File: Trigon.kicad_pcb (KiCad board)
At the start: 2 copper layers, 160 x 120 mm, 70 parts, among them J1 USB_C_Receptacle_USB2.0, SW1 SW_Push, SW2 Rotary_Encoder_Switch, U1 ATmega32U4-AU, Y1 16MHz

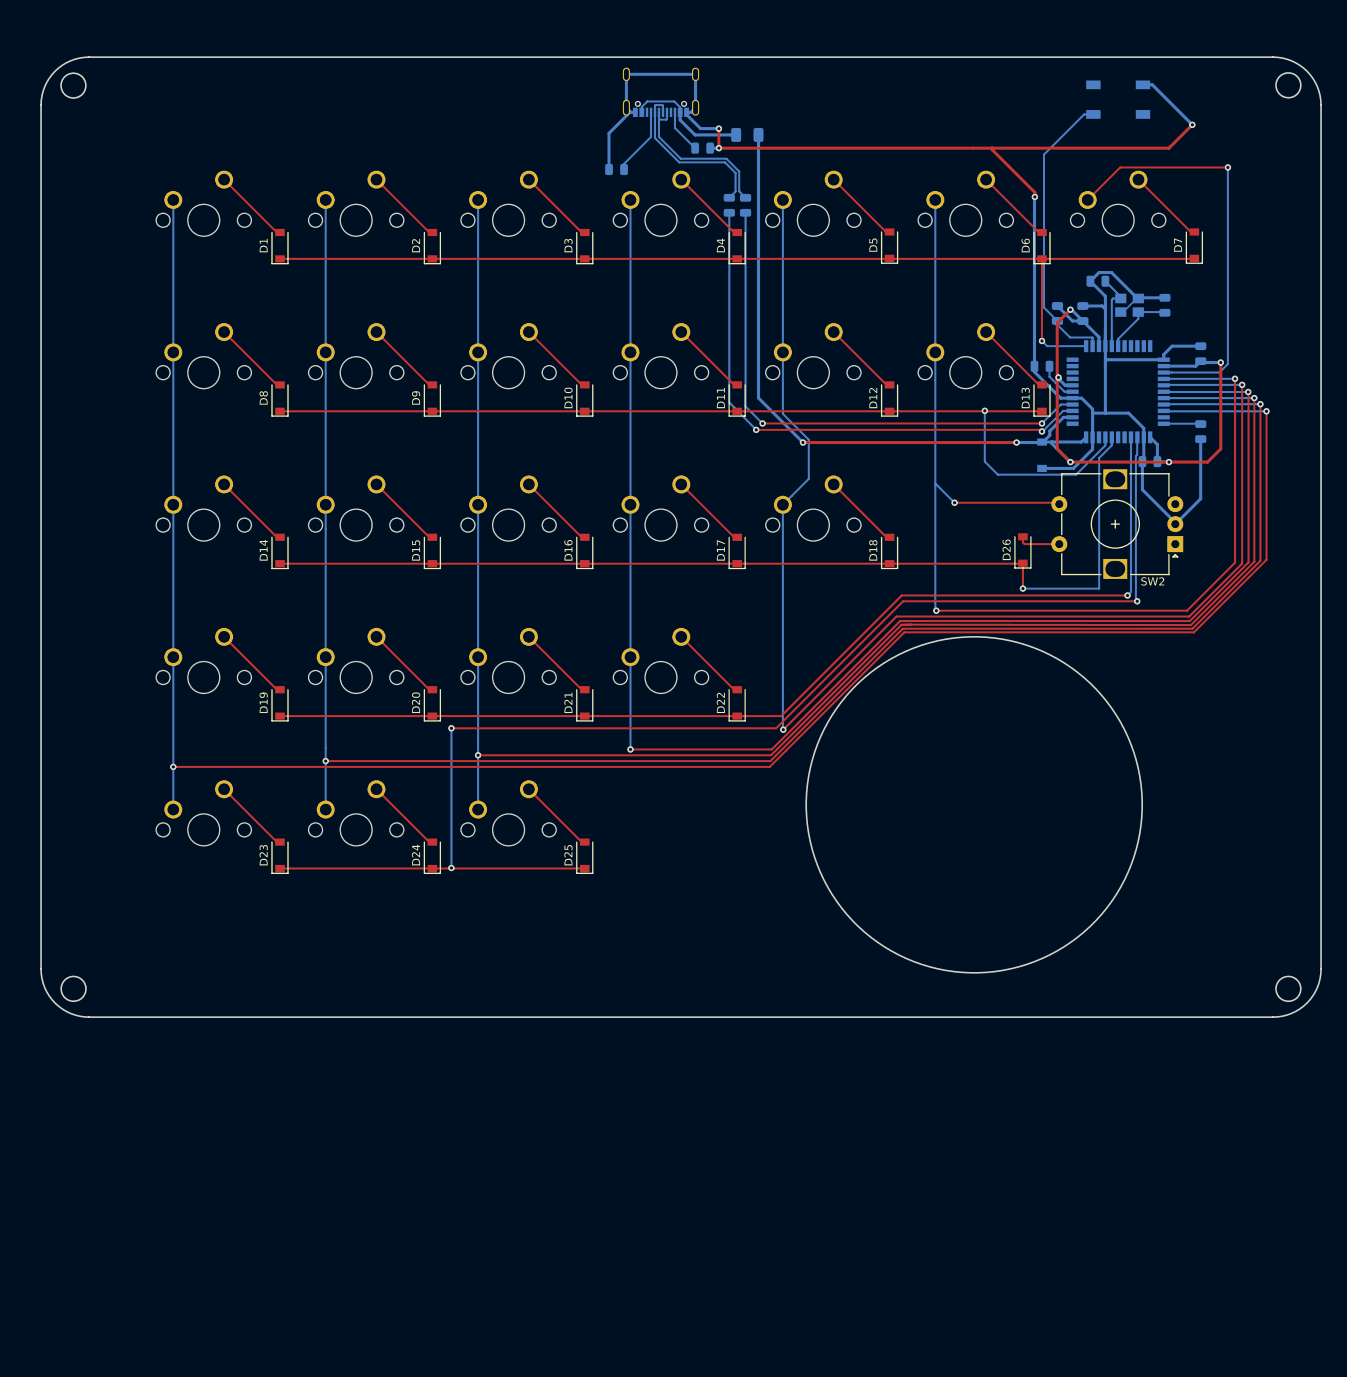
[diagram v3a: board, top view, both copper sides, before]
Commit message: full ground fill
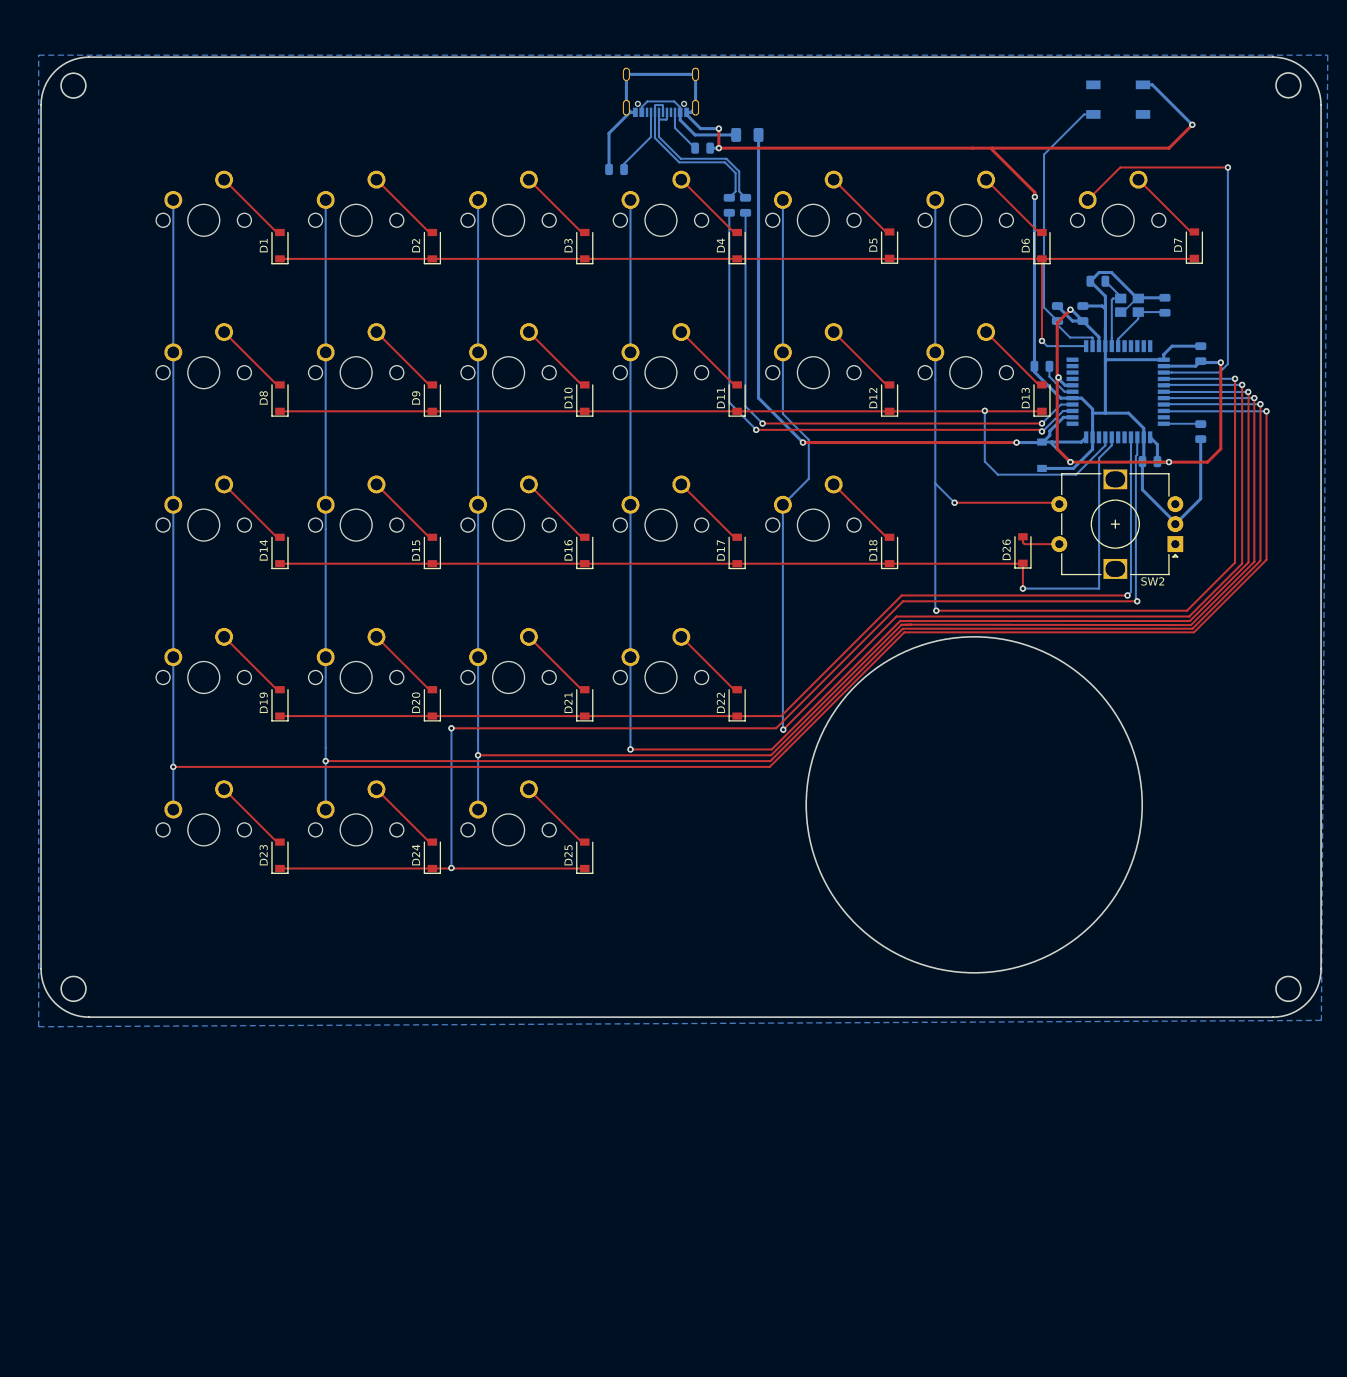
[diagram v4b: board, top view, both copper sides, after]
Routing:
- added copper zone on B.Cu, net (none)
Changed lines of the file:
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@@
   (segment (start 143.6215 -69.81875) (end 143.66875 -69.7715) (width 0.254) (layer B.Cu) (net 57))
   (segment (start 139.05 -69.81875) (end 143.6215 -69.81875) (width 0.254) (layer B.Cu) (net 57))
+  (zone (net 0) (net_name "") (layer B.Cu) (hatch edge 0.508)
+    (connect_pads (clearance 0.508))
+    (min_thickness 0.254)
+    (fill yes (arc_segments 32) (thermal_gap 0.508) (thermal_bridge_width 0.508))
+    (polygon
+      (pts
+        (xy 158.75 4.7625) (xy -1.5875 5.55625) (xy -1.5875 -115.8875) (xy 159.54375 -115.8875)
+      )
+    )
+  )
 )

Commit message: decorative stuff
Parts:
- added G***: LOGO, Trigon:wiggle-mask, B.Cu at (77.7, -57.7)
- added G***: LOGO, Trigon:wiggle, F.Cu at (78.0, -39.4)
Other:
- board text added: "by"
- board text added: "designed"
- board text added: "nk"
- board text added: "rev 0"

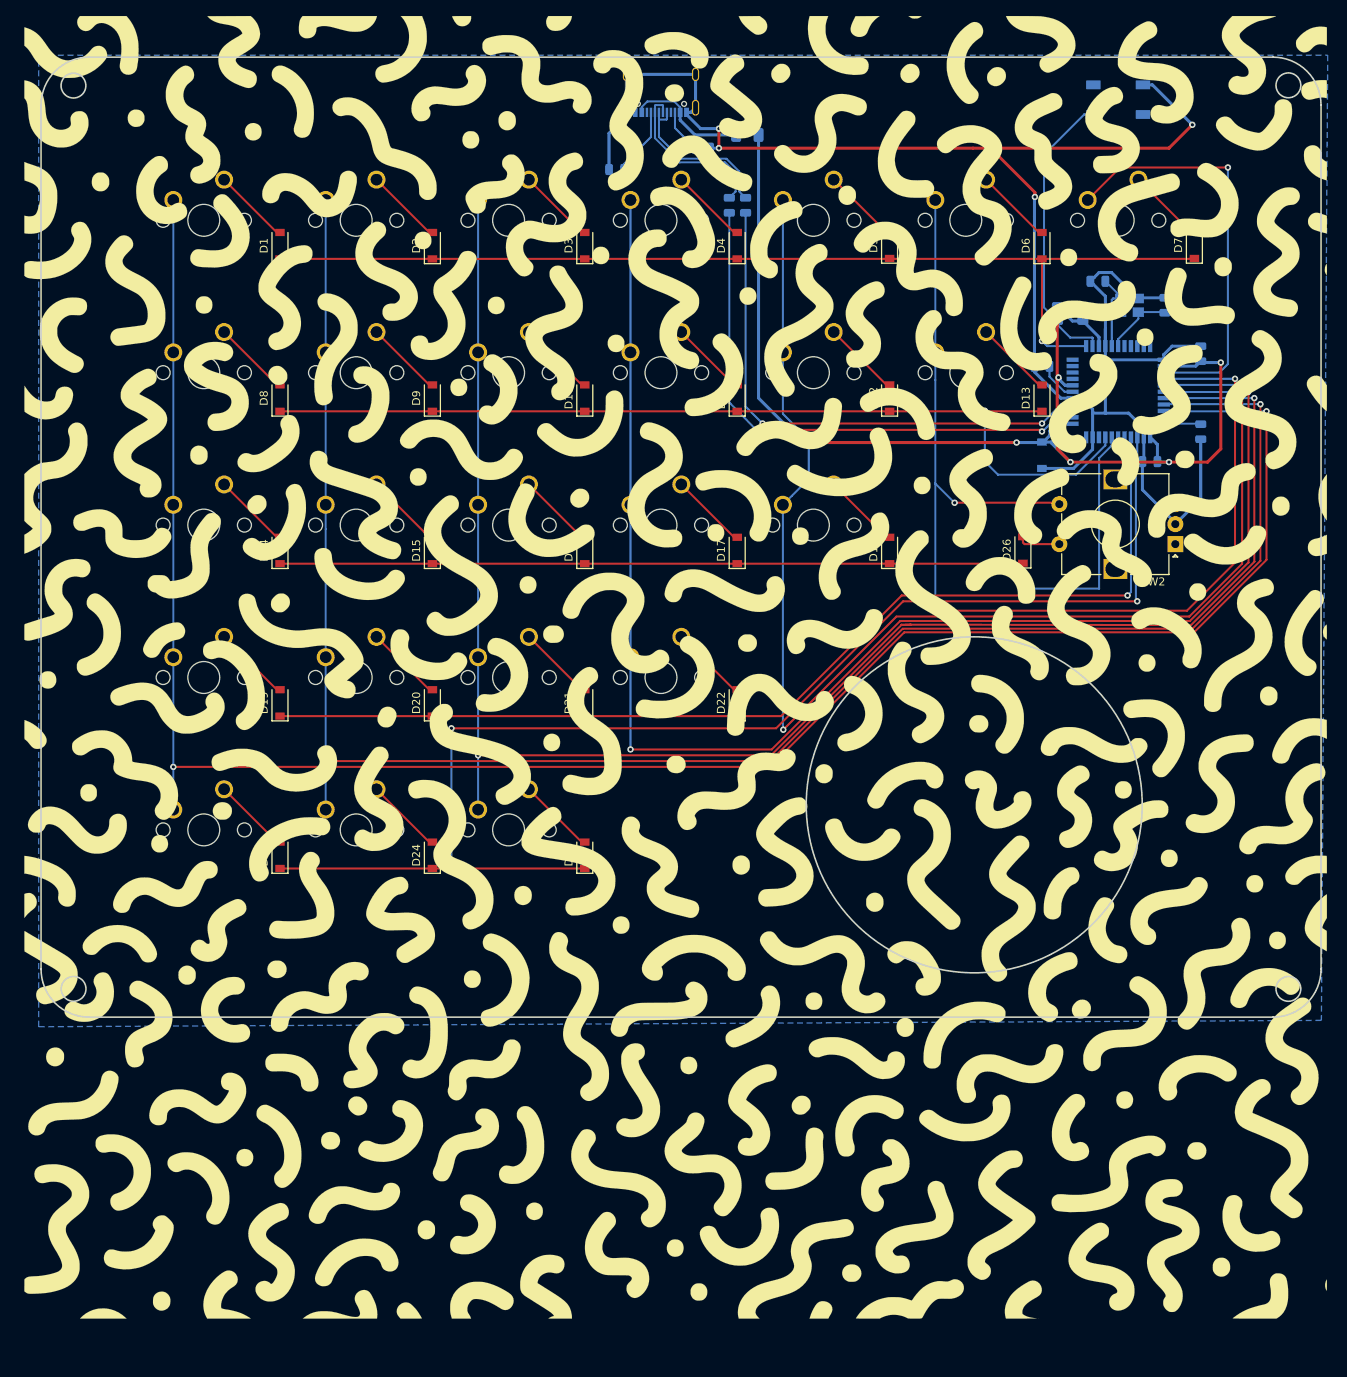
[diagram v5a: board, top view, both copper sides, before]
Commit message: all on one side
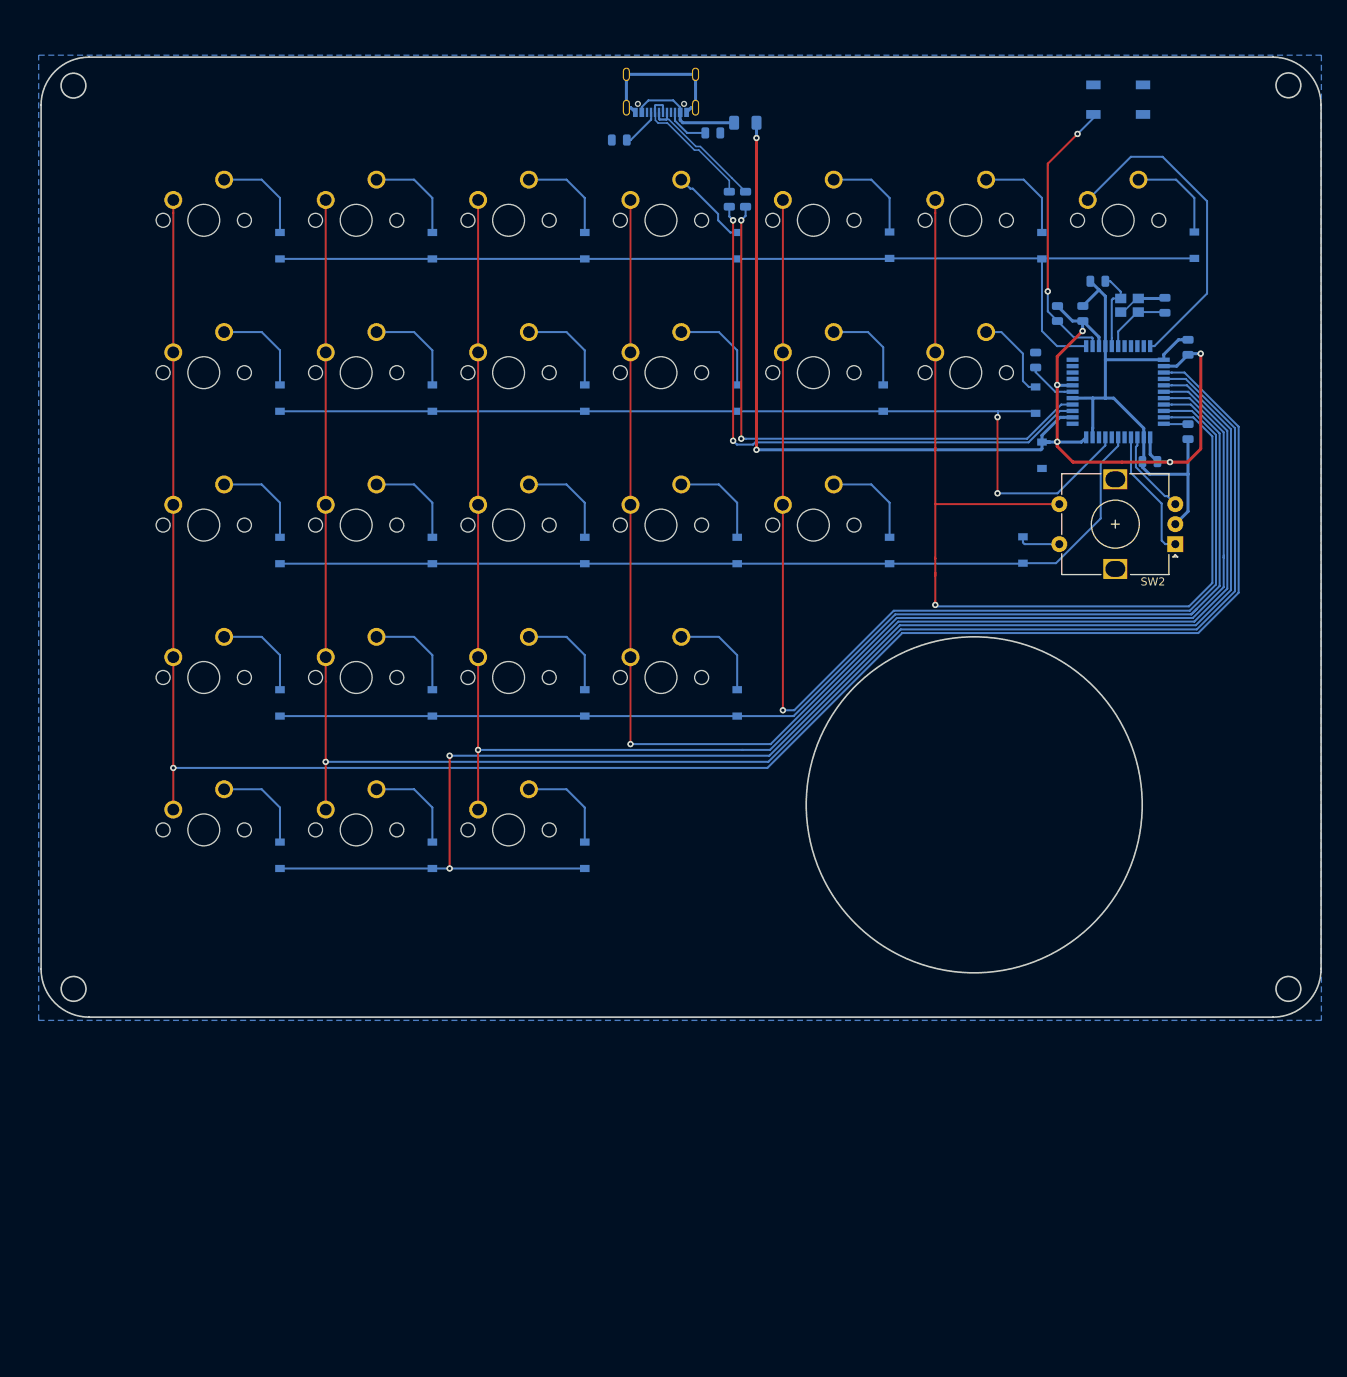
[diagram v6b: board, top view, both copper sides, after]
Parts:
- removed G***: LOGO, Trigon:wiggle-mask
- removed G***: LOGO, Trigon:wiggle
- D1, D10, D11, D12, D13, D14, D15, D16, D17, D18, D19, D2, D20, D21, D22, D23, D24, D25, D26, D3, D4, D5, D6, D7, D8, D9: moved to B.Cu
- moved R4 3.70 mm to (71.0, -105.3)
- moved R5 2.29 mm to (82.7, -106.2)
- moved C4 1.77 mm to (142.1, -79.4)
- moved R6 1.59 mm to (142.1, -68.8)
- moved F1 1.55 mm to (86.7, -107.4)
- moved C3 1.12 mm to (123.0, -77.8), turned to 90 degrees
- moved D13 0.83 mm to (123.0, -72.8)
- moved D12 0.79 mm to (104.0, -73.0)
- moved R1 0.76 mm to (86.8, -97.9)
- moved R2 0.76 mm to (84.7, -97.9)
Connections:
- U1 pad 22: Net-(U1-Pad22) -> COL6
- U1 pad 25: COL6 -> COL0
- U1 pad 26: COL5 -> COL1
- U1 pad 27: COL4 -> ROW4
- U1 pad 28: COL3 -> COL2
- U1 pad 29: COL2 -> COL3
- U1 pad 30: COL1 -> ROW3
- U1 pad 31: COL0 -> COL4
- U1 pad 32: Net-(U1-Pad32) -> COL5
- U1 pad 36: ROW4 -> ENC1A
- U1 pad 37: ROW3 -> ENC1B
- U1 pad 39: Net-(U1-Pad39) -> ROW2
- U1 pad 40: ROW2 -> Net-(U1-Pad40)
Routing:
- net GND: track 239.6 -> 93.6 mm, vias 4 -> 0
- net ROW4: track 168.6 -> 189.2 mm, vias 3 -> 2
- net ROW3: track 132.1 -> 152.7 mm, vias 1 -> 0
- net ENC1B: track 0.00 -> 16.4 mm
- net COL4: track 167.0 -> 150.9 mm, vias 2 -> 1
- net COL6: track 52.2 -> 40.8 mm, vias 1 -> 0
- net COL5: track 139.7 -> 128.4 mm, vias 3 -> 1
- net ENC1A: track 0.00 -> 10.6 mm
- net ROW2: track 125.2 -> 116.0 mm, vias 1 -> 0
- net COL3: track 187.7 -> 179.3 mm, vias 2 -> 1
- net COL2: track 216.5 -> 208.4 mm, vias 2 -> 1
- net Net-(R1-Pad1): track 66.9 -> 72.4 mm
- net COL1: track 235.4 -> 230.5 mm, vias 2 -> 1
- net Net-(R2-Pad1): track 70.0 -> 73.8 mm
- net D-: track 21.3 -> 17.5 mm
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- added copper zone on B.Cu, net GND
- removed copper zone on B.Cu, net (none)

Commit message: bring back masq
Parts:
- added G***: LOGO, Trigon:wiggle, F.Cu at (77.0, -34.1)
- added G***: LOGO, Trigon:wiggle-mask, B.Cu at (77.0, -34.1)

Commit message: cleaning up ground plane for solder mask layer
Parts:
- C7: footprint Diode_SMD:D_SOD-123 -> Capacitor_SMD:C_0805_2012Metric
- R4, R5: value R_Small -> 5.1k
- moved R5 6.84 mm to (76.2, -104.0)
- moved G*** 2.86 mm to (78.6, -36.5)
- moved G*** 2.25 mm to (78.6, -35.7)
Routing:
- net GND: track 93.6 -> 102.4 mm
- net Net-(J1-PadB5): track 5.46 -> 9.38 mm, vias 0 -> 2
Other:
- board text added: "Δkb"
- board text removed: "designed"
